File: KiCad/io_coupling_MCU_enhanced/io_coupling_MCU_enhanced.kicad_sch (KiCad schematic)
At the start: 57 parts, among them IC1 AP63205, IC2 AP2112K-3.3TRG1, J10 10PIN_HEADER, J2 Conn_Coaxial, J3 10PIN_HEADER, J4 10PIN_HEADER, J5 1987724, J6 1987724, J7 1987724, J8 1987724, J9 10PIN_HEADER, Q1 BSS138K-13/BSS159NH6327XTSA2, Q2 Si7469DP, Q3 BSS138K-13, Q4 BSS138K-13, Q5 BSS138K-13, Q6 RN2903, Q7 RN2903

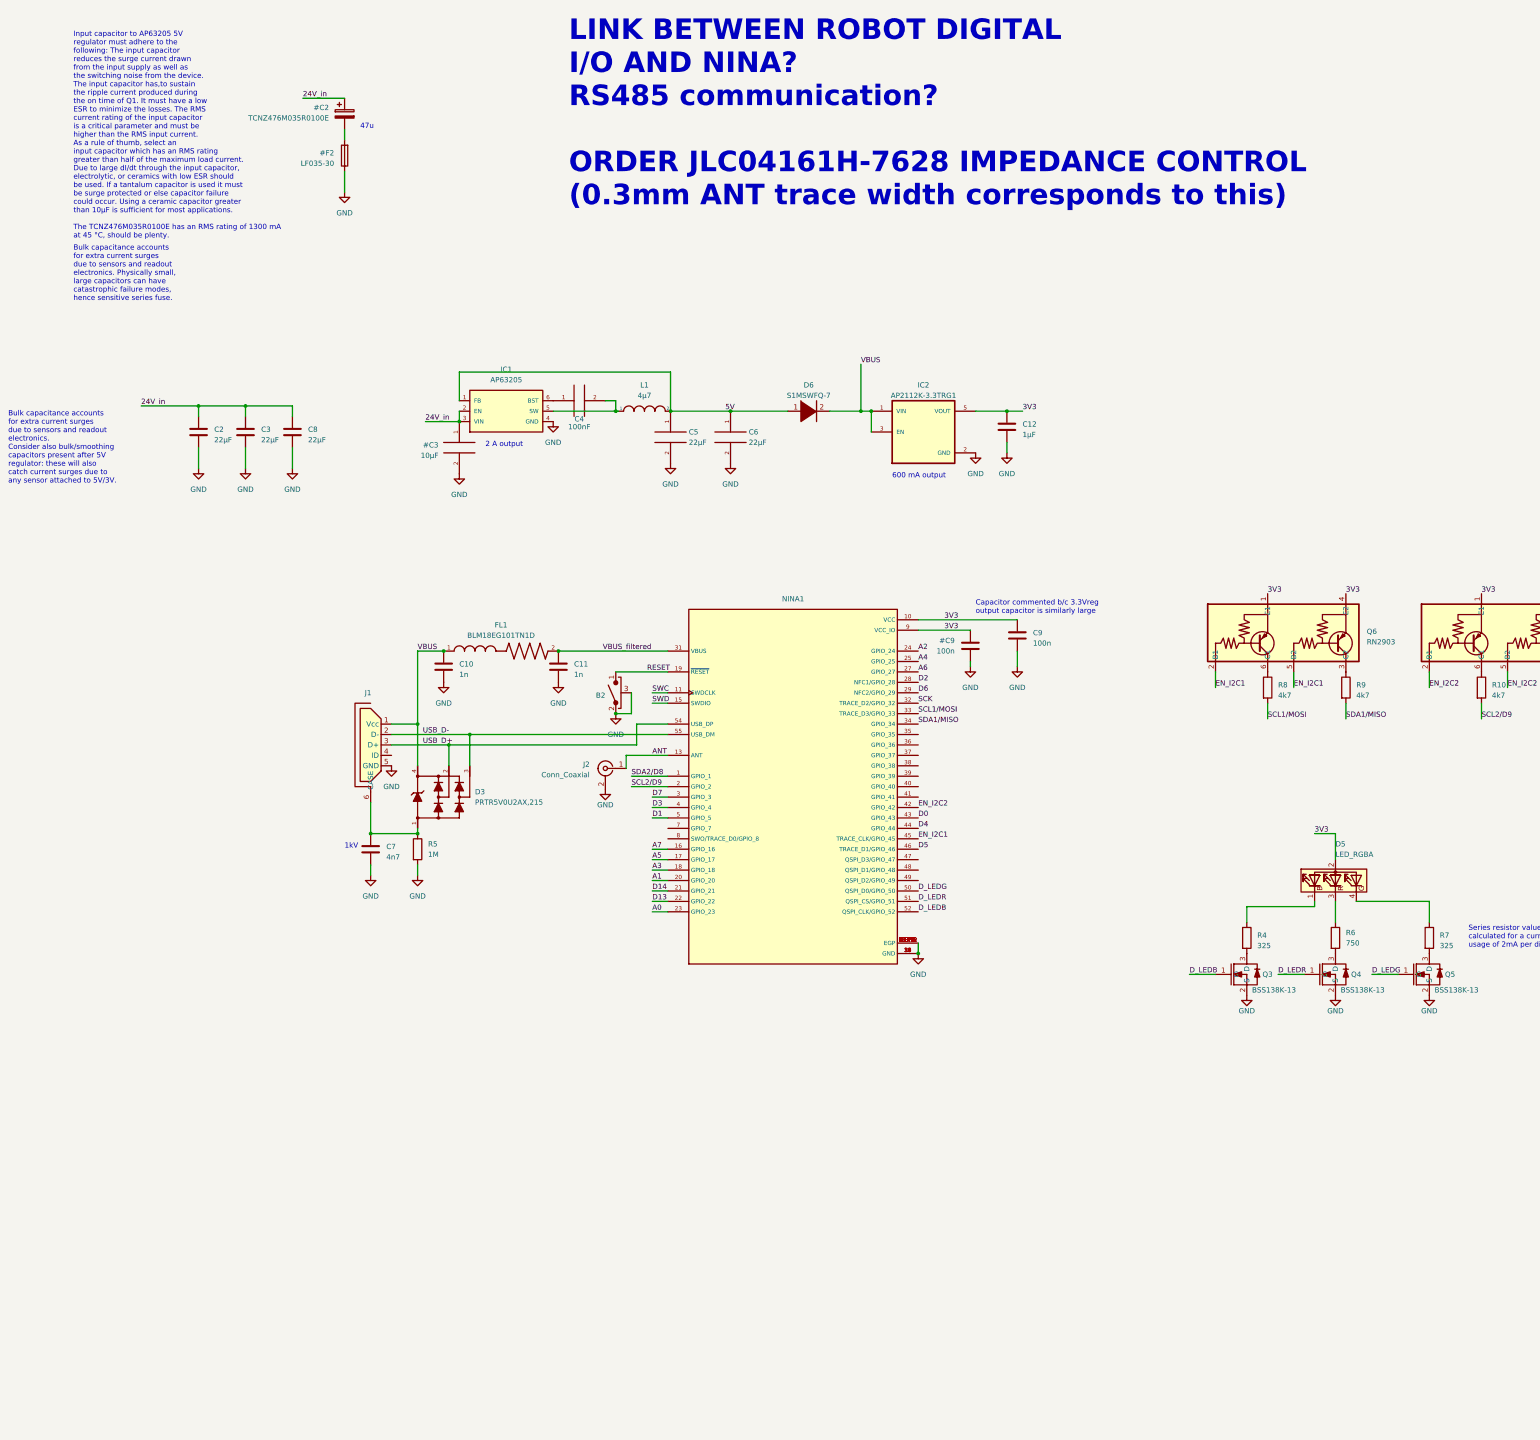
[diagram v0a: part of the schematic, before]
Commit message: fixed width of antenna trace
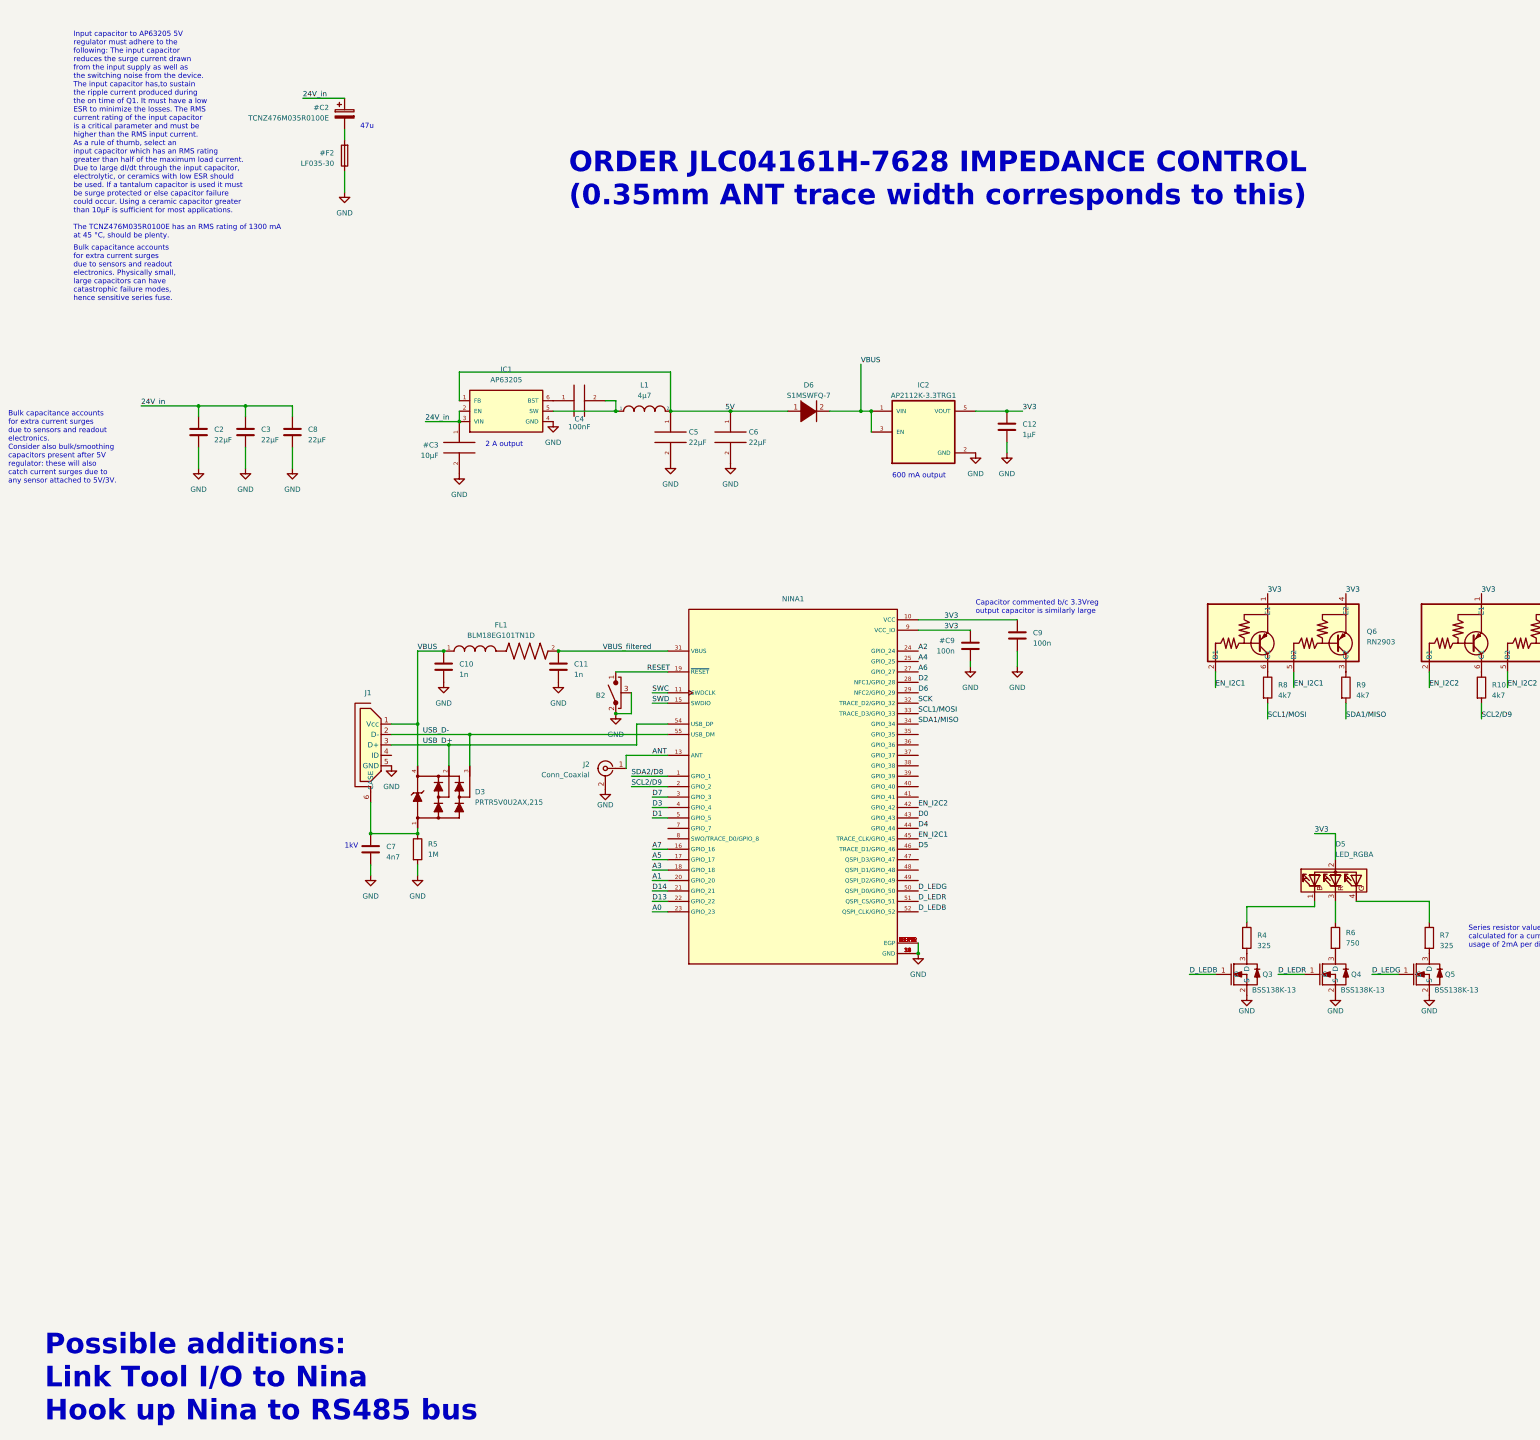
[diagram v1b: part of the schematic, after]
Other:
- note added: "ORDER JLC04161H-7628 IMPEDANCE CONTROL (0.35mm ANT trace width corresponds to this)"
- note added: "Possible additions: Link Tool I/O to Nina Hook up Nina to RS485 bus"
- note removed: "LINK BETWEEN ROBOT DIGITAL I/O AND NINA? RS485 communication? ORDER JLC04161H-7628 IMPEDANCE CONTROL (0.3mm ANT trace width corresponds to this)"
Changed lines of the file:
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@@
     (effects (font (size 1.27 1.27)) (justify left bottom))
   )
-  (text "LINK BETWEEN ROBOT DIGITAL\nI/O AND NINA?\nRS485 communication?\n\nORDER JLC04161H-7628 IMPEDANCE CONTROL\n(0.3mm ANT trace width corresponds to this)"
+  (text "ORDER JLC04161H-7628 IMPEDANCE CONTROL\n(0.35mm ANT trace width corresponds to this)"
     (at 157.48 78.74 0)
     (effects (font (size 5 5) (thickness 1) bold (color 255 0 6 1)) (justify left bottom))
@@
     (effects (font (size 1.27 1.27)) (justify left bottom))
   )
+  (text "Possible additions:\nLink Tool I/O to Nina\nHook up Nina to RS485 bus"
+    (at 29.845 374.65 0)
+    (effects (font (size 5 5) (thickness 1) bold (color 255 0 6 1)) (justify left bottom))
+  )
   (text "Series resistor values\ncalculated for a current\nusage of 2mA per diode"

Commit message: reworked annotations, removed kicad backup files
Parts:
- renumbered #C2 to #C1, #C3 to #C2, #C9 to #C3, #F2 to #F1, B2 to B1, C2 to C1, C12 to C10, C9 to C11, C1 to C12, C3 to C2, C8 to C3, C7 to C4, C10 to C5, C11 to C6, C4 to C7, C5 to C8, C6 to C9, D3 to D1, D6 to D2, D5 to D3, D1 to D4, D2 to D5, J4 to J10, J8 to J3, J7 to J4, J6 to J5, J5 to J6, J9 to J7, J10 to J8, J3 to J9, Q3 to Q1, Q6 to Q2, Q4 to Q3, Q5 to Q4, Q7 to Q5, Q1 to Q6, Q2 to Q7, R5 to R1, R2 to R10, R3 to R11, R4 to R2, R8 to R3, R6 to R4, R9 to R5, R7 to R6, R10 to R7, R11 to R8, R1 to R9

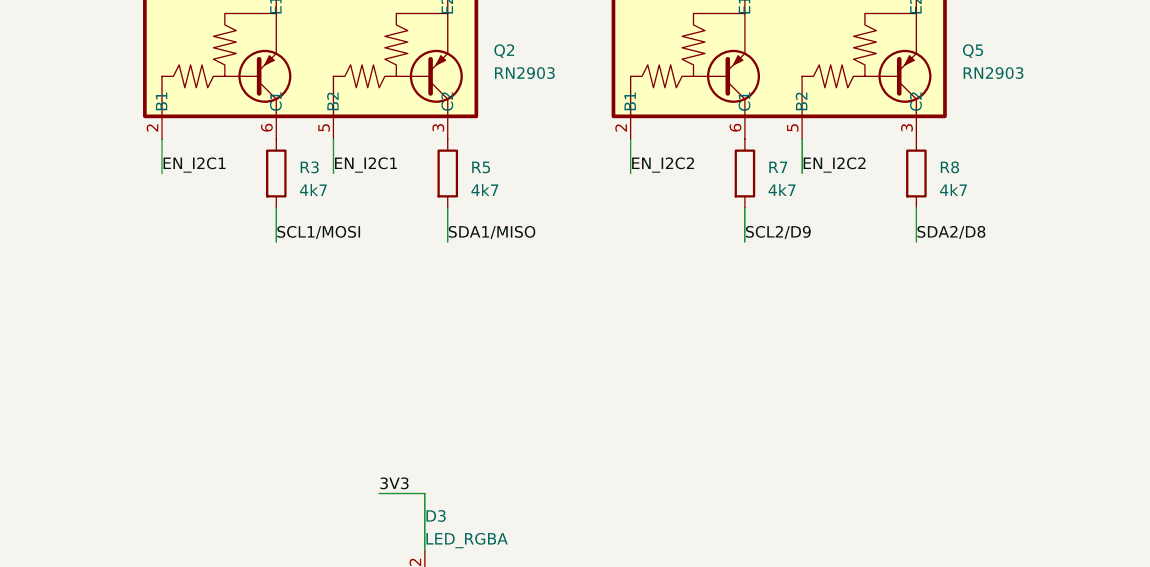
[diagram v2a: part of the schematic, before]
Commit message: added comment to schematic concerning I2C pullups
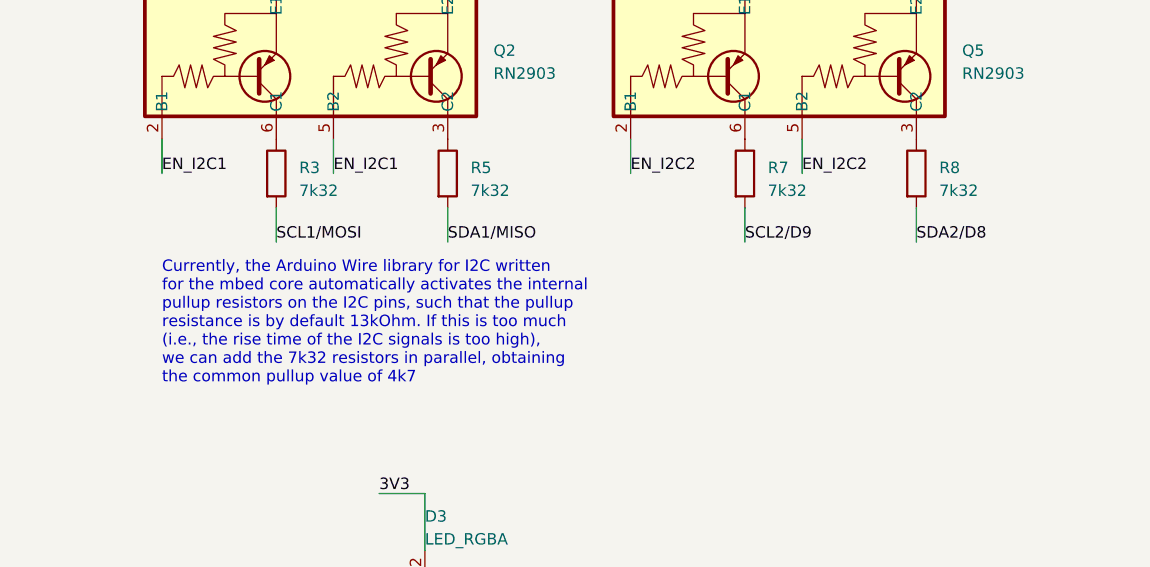
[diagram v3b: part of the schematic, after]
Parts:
- R3, R5, R7, R8: value 4k7 -> 7k32
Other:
- note added: "Currently, the Arduino Wire library for I2C written for the mbed core automatically activates the internal pullup resistors on the I2C pins, such that the pullup resistance is by default 13kOhm. If this is too much (i.e., the rise time of the I2C signals is too high), we can add the 7k32 resistors in parallel, obtaining the common pullup value of 4k7"
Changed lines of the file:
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@@
     (effects (font (size 1.27 1.27)) (justify left bottom))
+  )
+  (text "Currently, the Arduino Wire library for I2C written \nfor the mbed core automatically activates the internal\npullup resistors on the I2C pins, such that the pullup\nresistance is by default 13kOhm. If this is too much \n(i.e., the rise time of the I2C signals is too high),\nwe can add the 7k32 resistors in parallel, obtaining\nthe common pullup value of 4k7"
+    (at 314.96 219.075 0)
+    (effects (font (size 1.27 1.27) (color 255 19 74 1)) (justify left bottom))
   )
   (text "47u" (at 106.68 59.69 0)
@@
       (effects (font (size 1.27 1.27)) (justify left))
     )
-    (property "Value" "4k7" (at 382.27 197.485 0)
+    (property "Value" "7k32" (at 382.27 197.485 0)
       (effects (font (size 1.27 1.27)) (justify left))
     )
@@
       (effects (font (size 1.27 1.27)) (justify left))
     )
-    (property "Value" "4k7" (at 401.32 197.485 0)
+    (property "Value" "7k32" (at 401.32 197.485 0)
       (effects (font (size 1.27 1.27)) (justify left))
     )
@@
       (effects (font (size 1.27 1.27)) (justify left))
     )
-    (property "Value" "4k7" (at 330.2 197.485 0)
+    (property "Value" "7k32" (at 330.2 197.485 0)
       (effects (font (size 1.27 1.27)) (justify left))
     )
@@
       (effects (font (size 1.27 1.27)) (justify left))
     )
-    (property "Value" "4k7" (at 349.25 197.485 0)
-      (effects (font (size 1.27 1.27)) (justify left))
-    )
+    (property "Value" "7k32" (at 349.25 197.485 0)
+      (effects (font (size 1.27 1.27)) (justify left))
+    )

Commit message: added comment to schem
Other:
- note added: "Could be better to output Vbus instead of 5V, right now the 5V output is not available when only a microUSB connection is present and no 24V source."
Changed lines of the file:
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@@
     (effects (font (size 1.27 1.27)) (justify left bottom))
   )
-  (text "nMOSFET Q2 shorts GS of pMOSFET\nwhen Von is detached, so that \ngate of pMOSFET is rapidly discharged,\notherwise discharging takes about a second.\n(the gate of Q2 is pulled to 24V, as well as \nits drain. Now imagine any possible G-S\nvoltage at Q1 that would allow it to conduct:\nthis voltage would be shorted through the \nQ2 channel). Q2 is thought to be a BSS138, \nwhich is an enhancement mode MOSFET. I argue a \ndepletion mode MOSFET is more appropriate\nand propose a BSS126."
+  (text "nMOSFET Q2 shorts GS of pMOSFET\nwhen Von is detached, so that \ngate of pMOSFET is rapidly discharged,\notherwise discharging takes about a second.\n(the gate of Q2 is pulled to 24V, as well as \nits drain. Now imagine any possible G-S\nvoltage at Q1 that would allow it to conduct:\nthis voltage would be shorted through the \nQ2 channel). Q2 is thought to be a BSS138, \nwhich is an enhancement mode MOSFET. I argue a \ndepletion mode MOSFET is more appropriate\nand propose a BSS156."
     (at 518.16 185.42 0)
     (effects (font (size 1.27 1.27)) (justify left bottom))
@@
     (effects (font (size 1.27 1.27)) (justify left bottom))
   )
+  (text "Could be better to output Vbus instead of 5V, \nright now the 5V output is not available when \nonly a microUSB connection is present and \nno 24V source."
+    (at 474.98 233.68 0)
+    (effects (font (size 1.27 1.27) (color 255 19 74 1)) (justify left bottom))
+  )
   (label "D7" (at 177.8 222.25 0) (fields_autoplaced)

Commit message: prettified schematic
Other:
- note added: "Features"
- note added: "I/O"
- note added: "Maybe attach VBUS_filtered here instead of VBUS"
- note added: "Microcontroller"
- note added: "Original Robotiq I/O Coupling safety circuit"
- note added: "Power"
- moved on the sheet: B1, C1, C10, C11, C12, C2, C3, C4, C5, C6, C7, C8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
